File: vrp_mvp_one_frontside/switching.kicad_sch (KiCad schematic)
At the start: 12 parts, among them Q1 MMBT2222A, Q2 MMBT2222A, Q3 MMBT2222A

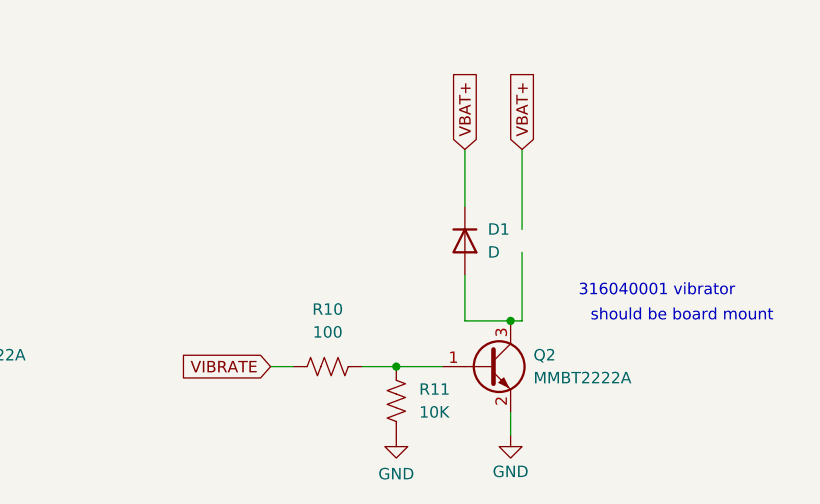
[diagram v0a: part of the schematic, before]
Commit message: removed vibration motor circuitry
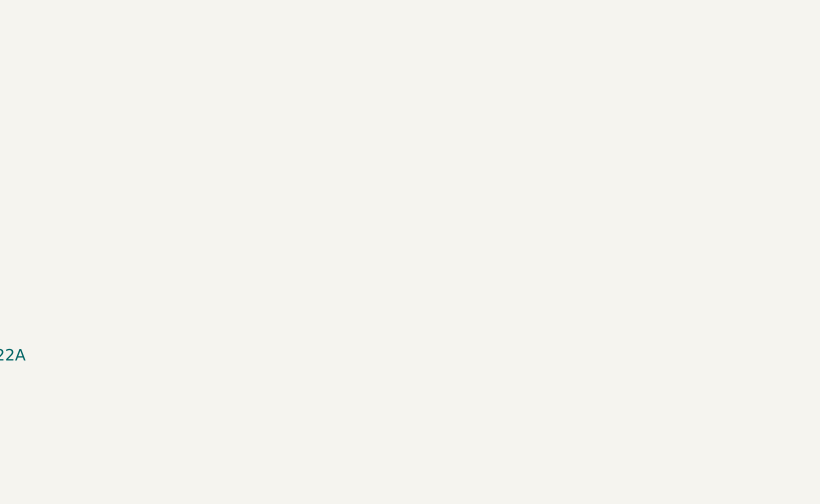
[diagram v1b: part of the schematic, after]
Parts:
- removed D1: D, symbol Device:D
- removed Q2: MMBT2222A, Package_TO_SOT_SMD:SOT-23_Handsoldering, symbol Transistor_BJT:MMBT2222A
- removed R10: 100, Resistor_SMD:R_0805_2012Metric_Pad1.20x1.40mm_HandSolder, symbol Device:R_US
- removed R11: 10K, Resistor_SMD:R_0805_2012Metric_Pad1.20x1.40mm_HandSolder, symbol Device:R_US
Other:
- note removed: "316040001 vibrator"
- note removed: "should be board mount"
